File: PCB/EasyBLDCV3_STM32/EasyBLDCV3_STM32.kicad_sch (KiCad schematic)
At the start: 0 parts

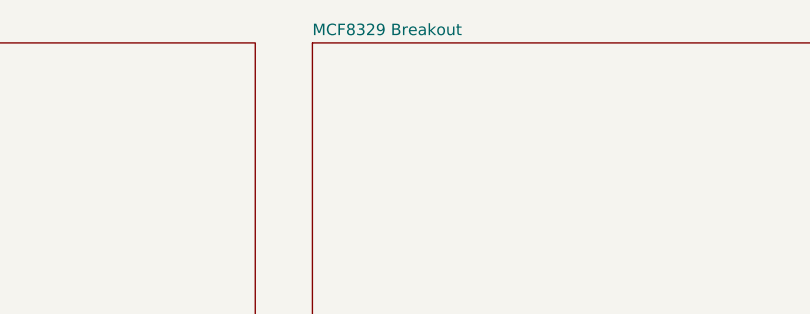
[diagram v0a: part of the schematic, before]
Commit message: Added footprints and began schematic for new gate drive
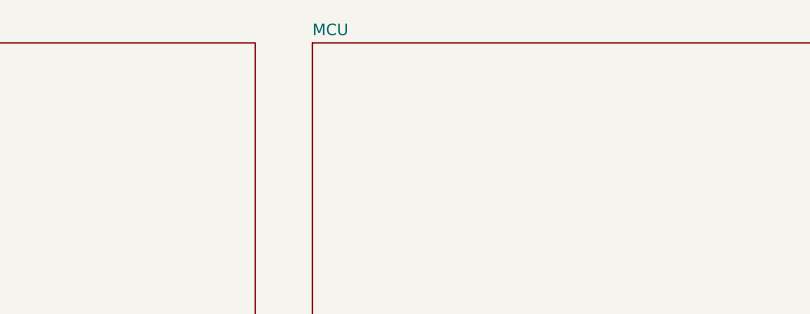
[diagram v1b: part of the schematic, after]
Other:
- sheet MCF8329 Breakout renamed MCU
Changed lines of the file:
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@@
 			(color 0 0 0 0.0000)
 		)
-		(property "Sheetname" "MCF8329 Breakout"
+		(property "Sheetname" "MCU"
 			(at 191.77 61.5184 0)
 			(effects
